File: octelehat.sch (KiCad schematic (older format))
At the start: 32 parts, among them J1 GROVE-CONNECTOR-DIP-90D_4P-2.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, J2 GROVE-CONNECTOR-DIP-90D_4P-2.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, J3 GROVE-CONNECTOR-DIP-90D_4P-2.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, P1 CONN_02X20, P2 CONN_01X02, P3 CONN_01X02, U1 MAX31855KASA, U2 ADS1015, U3 MAX31855KASA

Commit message: work in progress
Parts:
- P1: MFPN F185-1220A0BSYA1 -> (none); MPN (none) -> F185-1220A0BSYA1
- U2: MPN (none) -> ADS1015IDGSR; Manufacturer (none) -> Texas Instruments
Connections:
- net +3V3: now also J1.3, J2.3
- net GND: now also J1.4, J2.4
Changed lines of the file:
@@
 F 3 "https://statics3.seeedstudio.com/images/opl/datasheet/320030087.pdf" H 2400 1400 50  0001 C CNN
 F 4 "YXCON" H 2400 2350 60  0001 C CNN "Manufacturer"
-F 5 "F185-1220A0BSYA1" H 2400 1300 50  0000 C CNN "MFPN"
+F 5 "F185-1220A0BSYA1" H 2400 1300 50  0000 C CNN "MPN"
 	1    2400 2350
 	1    0    0    -1
@@
 F 2 "Housings_SSOP:TSSOP-10_3x3mm_Pitch0.5mm" H 7550 4100 60  0001 C CNN
 F 3 "http://www.ti.com/lit/ds/symlink/ads1015.pdf" H 7550 4100 60  0001 C CNN
+F 4 "ADS1015IDGSR" H 7550 4100 60  0001 C CNN "MPN"
+F 5 "Texas Instruments" H 7550 4100 60  0001 C CNN "Manufacturer"
 	1    7550 4100
 	1    0    0    -1
@@
 	3850 7400 3850 6750
 Wire Wire Line
-	3850 6750 4000 6750
-Wire Wire Line
-	4000 6650 3800 6650
+	3400 6750 4000 6750
+Wire Wire Line
+	3400 6650 4000 6650
 Wire Wire Line
 	3800 6650 3800 7300
@@
 Wire Wire Line
 	8100 5900 10450 5900
+Connection ~ 3800 6650
+Connection ~ 3850 6750
+Text Label 3400 6650 2    60   ~ 0
++3V3
+Text Label 3400 6750 2    60   ~ 0
+GND
 $EndSCHEMATC

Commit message: rev1 routing
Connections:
- net at C8.2, C9.1, R7.1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: now also R8.1; no longer J3.2
- net at C7.2, C8.1, R7.2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: now also J3.2; no longer R8.1
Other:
- moved on the sheet: R8
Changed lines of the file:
@@
 	8550 4200 8550 4850
 Wire Wire Line
-	8550 4850 9500 4850
+	8550 4850 10250 4850
 Wire Wire Line
 	8800 4800 8800 4900
@@
 	9300 5250 9300 5200
 Connection ~ 9300 5250
-Wire Wire Line
-	9800 4850 10350 4850
 $Comp
 L GND #PWR018
@@
 Text Label 2650 1400 0    60   ~ 0
 5V
-Wire Wire Line
-	8450 5250 10250 5250
 Wire Notes Line
 	3800 700  950  700
@@
 $EndComp
 Wire Wire Line
-	10250 5250 10250 5700
-Wire Wire Line
 	10250 5700 10450 5700
-Wire Wire Line
-	10350 4850 10350 5600
 Wire Wire Line
 	10350 5600 10450 5600
@@
 L SMD-RES-30K-1%-1_10W_0603_ R8
 U 1 1 58E635B8
-P 9650 4850
-F 0 "R8" H 9500 4900 45  0000 L BNN
-F 1 "SMD-RES-30K-1%-1_10W_0603_" H 9650 4900 45  0000 L BNN
-F 2 "SeeedOPL-Resistor-2016:R0603" H 9650 4850 40  0001 C CNN
-F 3 "" H 9650 4850 40  0001 C CNN
-F 4 "RC0603FR-0730KL" H 9680 5000 20  0001 C CNN "MPN"
-F 5 "301010202" H 9680 5000 20  0001 C CNN "SKU"
-	1    9650 4850
+P 9650 5250
+F 0 "R8" H 9500 5300 45  0000 L BNN
+F 1 "SMD-RES-30K-1%-1_10W_0603_" H 9650 5300 45  0000 L BNN
+F 2 "SeeedOPL-Resistor-2016:R0603" H 9650 5250 40  0001 C CNN
+F 3 "" H 9650 5250 40  0001 C CNN
+F 4 "RC0603FR-0730KL" H 9680 5400 20  0001 C CNN "MPN"
+F 5 "301010202" H 9680 5400 20  0001 C CNN "SKU"
+	1    9650 5250
 	1    0    0    -1
 $EndComp
@@
 Text Label 3400 6750 2    60   ~ 0
 GND
+Wire Wire Line
+	8450 5250 9500 5250
+Wire Wire Line
+	9800 5250 10350 5250
+Wire Wire Line
+	10350 5250 10350 5600
+Wire Wire Line
+	10250 4850 10250 5700
 $EndSCHEMATC

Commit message: revised
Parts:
- C1, C10, C2, C3, C4, C6, C7, C8, C9: OPL 302010024 -> (none); SKU (none) -> 302010024
- C11, C5: OPL 302010006 -> (none); SKU (none) -> 302010006
- FB1, FB2, FB3, FB4: OPL 303030001 -> (none); SKU (none) -> 303030001
- J1, J2, J3: OPL 320110034 -> (none); SKU (none) -> 320110034
- P1: SKU (none) -> 320030015
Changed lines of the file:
@@
 Sheet 1 1
 Title "Overclocking Telemetry HAT for Raspberry Pi 3"
-Date "2017-04-05"
-Rev "v1"
+Date "2017-04-07"
+Rev "1"
 Comp "moonpunch.org"
 Comment1 "CERN OHL 1.2"
@@
 F 4 "YXCON" H 2400 2350 60  0001 C CNN "Manufacturer"
 F 5 "F185-1220A0BSYA1" H 2400 1300 50  0000 C CNN "MPN"
+F 6 "320030015" H 2400 2350 60  0001 C CNN "SKU"
 	1    2400 2350
 	1    0    0    -1
@@
 F 4 "Yageo" H 6550 2000 60  0001 C CNN "Manufacturer"
 F 5 "CC0402KRX7R9BB103" H 6550 2000 60  0001 C CNN "MPN"
-F 6 "302010006" H 6550 2000 60  0001 C CNN "OPL"
+F 6 "302010006" H 6550 2000 60  0001 C CNN "SKU"
 	1    6550 2000
 	-1   0    0    -1
@@
 F 4 "Yageo" H 6100 1400 60  0001 C CNN "Manufacturer"
 F 5 "CC0402KRX7R8BB104" H 6100 1400 60  0001 C CNN "MPN"
-F 6 "302010024" H 6100 1400 60  0001 C CNN "OPL"
+F 6 "302010024" H 6100 1400 60  0001 C CNN "SKU"
 	1    6100 1400
 	0    -1   -1   0
@@
 F 4 "Murata" H 6900 1800 60  0001 C CNN "Manufacturer"
 F 5 "BLM18AG121SN1D" H 6750 1550 50  0000 C CNN "MPN"
-F 6 "303030001" H 6900 1800 60  0001 C CNN "OPL"
+F 6 "303030001" H 6900 1800 60  0001 C CNN "SKU"
 F 7 "Taiyo Yuden" H 6900 1800 60  0001 C CNN "Manufacturer2"
 F 8 "BK1608HW121-T" H 6800 1550 40  0001 C CNN "MPN2"
@@
 F 4 "Murata" H 6900 2200 60  0001 C CNN "Manufacturer"
 F 5 "BLM18AG121SN1D" H 6900 2200 60  0001 C CNN "MPN"
-F 6 "303030001" H 6900 2200 60  0001 C CNN "OPL"
+F 6 "303030001" H 6900 2200 60  0001 C CNN "SKU"
 F 7 "Taiyo Yuden" H 6900 2200 60  0001 C CNN "Manufacturer2"
 F 8 "BK1608HW121-T" H 6800 1950 40  0001 C CNN "MPN2"
@@
 F 4 "Murata" H 10250 1800 60  0001 C CNN "Manufacturer"
 F 5 "BLM18AG121SN1D" H 10050 1550 50  0000 C CNN "MPN"
-F 6 "303030001" H 10250 1800 60  0001 C CNN "OPL"
+F 6 "303030001" H 10250 1800 60  0001 C CNN "SKU"
 F 7 "Taiyo Yuden" H 10250 1800 60  0001 C CNN "Manufacturer2"
 F 8 "BK1608HW121-T" H 10150 1550 40  0001 C CNN "MPN2"
@@
 F 4 "Murata" H 10250 2200 60  0001 C CNN "Manufacturer"
 F 5 "BLM18AG121SN1D" H 10250 2200 60  0001 C CNN "MPN"
-F 6 "303030001" H 10250 2200 60  0001 C CNN "OPL"
+F 6 "303030001" H 10250 2200 60  0001 C CNN "SKU"
 F 7 "Taiyo Yuden" H 10250 2200 60  0001 C CNN "Manufacturer2"
 F 8 "BK1608HW121-T" H 10150 1950 40  0001 C CNN "MPN2"
@@
 F 4 "Yageo" H 9900 2000 60  0001 C CNN "Manufacturer"
 F 5 "CC0402KRX7R9BB103" H 9900 2000 60  0001 C CNN "MPN"
-F 6 "302010006" H 9900 2000 60  0001 C CNN "OPL"
+F 6 "302010006" H 9900 2000 60  0001 C CNN "SKU"
 	1    9900 2000
 	-1   0    0    -1
@@
 F 4 "Yageo" H 9450 1400 60  0001 C CNN "Manufacturer"
 F 5 "CC0402KRX7R8BB104" H 9450 1400 60  0001 C CNN "MPN"
-F 6 "302010024" H 9450 1400 60  0001 C CNN "OPL"
+F 6 "302010024" H 9450 1400 60  0001 C CNN "SKU"
 	1    9450 1400
 	0    -1   -1   0
@@
 F 4 "Yageo" H 6150 4800 60  0001 C CNN "Manufacturer"
 F 5 "CC0402KRX7R8BB104" H 6150 4800 60  0001 C CNN "MPN"
-F 6 "302010024" H 6150 4800 60  0001 C CNN "OPL"
+F 6 "302010024" H 6150 4800 60  0001 C CNN "SKU"
 	1    6150 4800
 	1    0    0    -1
@@
 F 4 "Yageo" H 8800 4250 60  0001 C CNN "Manufacturer"
 F 5 "CC0402KRX7R8BB104" H 8800 4250 60  0001 C CNN "MPN"
-F 6 "302010024" H 8800 4250 60  0001 C CNN "OPL"
+F 6 "302010024" H 8800 4250 60  0001 C CNN "SKU"
 	1    8800 4250
 	1    0    0    -1
@@
 F 4 "Taifeng" H 10600 5750 60  0001 C CNN "Manufacturer"
 F 5 "1125R-4P" H 10600 5750 60  0001 C CNN "MPN"
-F 6 "320110034" H 10630 5900 20  0001 C CNN "OPL"
+F 6 "320110034" H 10630 5900 20  0001 C CNN "SKU"
 	1    10600 5750
 	1    0    0    -1
@@
 F 4 "Yageo" H 8800 4650 60  0001 C CNN "Manufacturer"
 F 5 "CC0402KRX7R8BB104" H 8800 4650 60  0001 C CNN "MPN"
-F 6 "302010024" H 8800 4650 60  0001 C CNN "OPL"
+F 6 "302010024" H 8800 4650 60  0001 C CNN "SKU"
 	1    8800 4650
 	1    0    0    -1
@@
 F 4 "Yageo" H 8800 5050 60  0001 C CNN "Manufacturer"
 F 5 "CC0402KRX7R8BB104" H 8800 5050 60  0001 C CNN "MPN"
-F 6 "302010024" H 8800 5050 60  0001 C CNN "OPL"
+F 6 "302010024" H 8800 5050 60  0001 C CNN "SKU"
 	1    8800 5050
 	1    0    0    -1
@@
 F 4 "Yageo" H 8800 5450 60  0001 C CNN "Manufacturer"
 F 5 "CC0402KRX7R8BB104" H 8800 5450 60  0001 C CNN "MPN"
-F 6 "302010024" H 8800 5450 60  0001 C CNN "OPL"
+F 6 "302010024" H 8800 5450 60  0001 C CNN "SKU"
 	1    8800 5450
 	1    0    0    -1
@@
 F 4 "Yageo" H 6150 5200 60  0001 C CNN "Manufacturer"
 F 5 "CC0402KRX7R8BB104" H 6150 5200 60  0001 C CNN "MPN"
-F 6 "302010024" H 6150 5200 60  0001 C CNN "OPL"
+F 6 "302010024" H 6150 5200 60  0001 C CNN "SKU"
 	1    6150 5200
 	1    0    0    -1
@@
 F 4 "Yageo" H 6150 5600 60  0001 C CNN "Manufacturer"
 F 5 "CC0402KRX7R8BB104" H 6150 5600 60  0001 C CNN "MPN"
-F 6 "302010024" H 6150 5600 60  0001 C CNN "OPL"
+F 6 "302010024" H 6150 5600 60  0001 C CNN "SKU"
 	1    6150 5600
 	1    0    0    -1
@@
 F 4 "Taifeng" H 4150 6600 60  0001 C CNN "Manufacturer"
 F 5 "1125R-4P" H 4150 6600 60  0001 C CNN "MPN"
-F 6 "320110034" H 4180 6750 20  0001 C CNN "OPL"
+F 6 "320110034" H 4180 6750 20  0001 C CNN "SKU"
 	1    4150 6600
 	1    0    0    -1
@@
 F 4 "Taifeng" H 4150 7250 60  0001 C CNN "Manufacturer"
 F 5 "1125R-4P" H 4150 7250 60  0001 C CNN "MPN"
-F 6 "320110034" H 4180 7400 20  0001 C CNN "OPL"
+F 6 "320110034" H 4180 7400 20  0001 C CNN "SKU"
 	1    4150 7250
 	1    0    0    -1

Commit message: design update
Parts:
- FB1, FB2, FB3, FB4: footprint Resistors_SMD:R_0603_HandSoldering -> SeeedOPL-Inductor-2016:L0603
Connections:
- net at C3.2, C4.1, R3.1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: now also J3.2; no longer J3.4
- net at C7.2, C8.1, R7.2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: now also J3.4; no longer J3.2
- net at J3.1: now also R4.2; no longer R8.2
- net at J3.3: now also R8.2; no longer R4.2

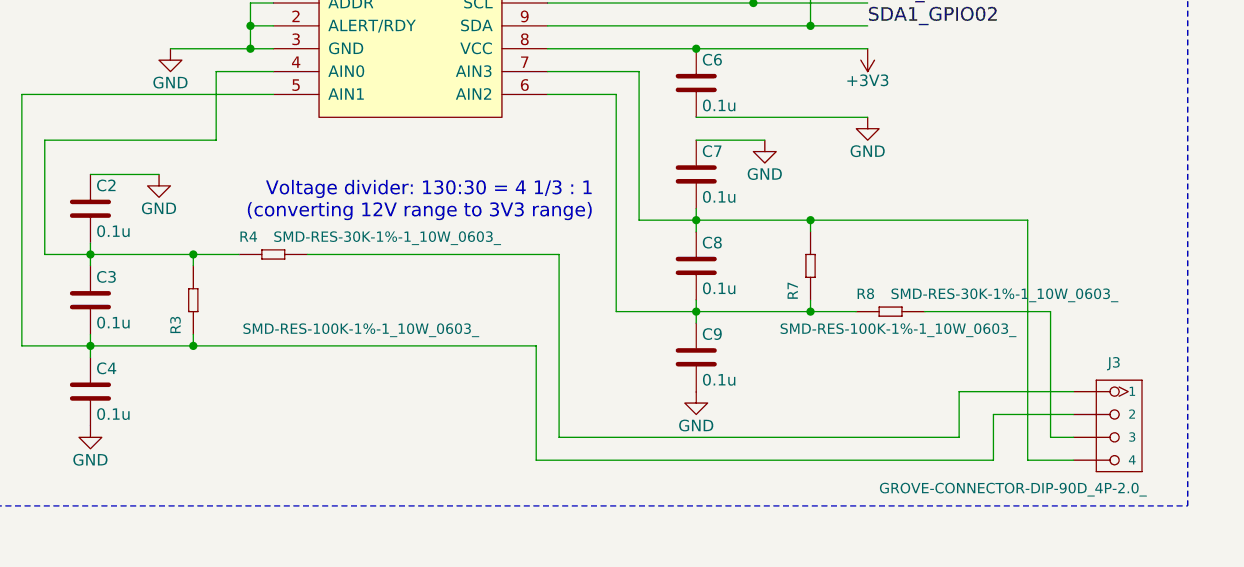
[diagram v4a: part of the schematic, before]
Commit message: update voltage divider part of circuit
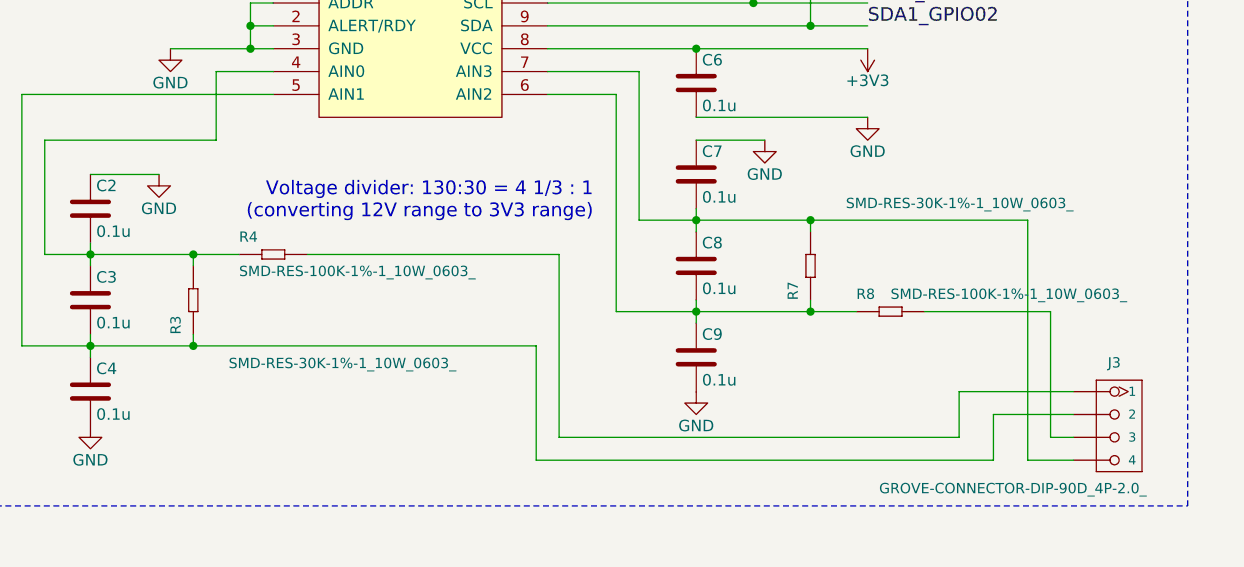
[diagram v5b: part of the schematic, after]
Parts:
- removed R3, R7: SMD-RES-100K-1%-1_10W_0603_, SeeedOPL-Resistor-2016:R0603, symbol SMD-RES-100K-1%-1_10W_0603_
- removed R4, R8: SMD-RES-30K-1%-1_10W_0603_, SeeedOPL-Resistor-2016:R0603, symbol SMD-RES-30K-1%-1_10W_0603_
- added R3, R7: SMD-RES-30K-1%-1_10W_0603_, symbol SMD-RES-30K-1%-1_10W_0603_
- added R4, R8: SMD-RES-100K-1%-1_10W_0603_, symbol SMD-RES-100K-1%-1_10W_0603_
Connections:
- net at C2.2, C3.1, U2.4 (AIN0): now also R3.2, R4.1
- net at C3.2, C4.1, J3.2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: now also R3.1
- net at C8.2, C9.1, U2.6 (AIN2): now also R7.1, R8.1
- net at C7.2, C8.1, J3.4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: now also R7.2
- net at J3.1: now also R4.2
- net at J3.3: now also R8.2
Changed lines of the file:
@@
 Sheet 1 1
 Title "Overclocking Telemetry HAT for Raspberry Pi 3"
-Date "2017-04-10"
-Rev "1"
+Date "2017-05-19"
+Rev "2"
 Comp "moonpunch.org"
 Comment1 "CERN OHL 1.2"
@@
 $EndComp
 $Comp
-L SMD-RES-30K-1%-1_10W_0603_ R4
-U 1 1 58E62ECC
-P 6950 5000
-F 0 "R4" H 6800 5050 45  0000 L BNN
-F 1 "SMD-RES-30K-1%-1_10W_0603_" H 6950 5050 45  0000 L BNN
-F 2 "SeeedOPL-Resistor-2016:R0603" H 6950 5000 40  0001 C CNN
-F 3 "" H 6950 5000 40  0001 C CNN
-F 4 "RC0603FR-0730KL" H 6980 5150 20  0001 C CNN "MPN"
-F 5 "301010202" H 6980 5150 20  0001 C CNN "SKU"
-	1    6950 5000
-	1    0    0    -1
-$EndComp
-$Comp
-L SMD-RES-100K-1%-1_10W_0603_ R3
-U 1 1 58E63018
-P 6600 5200
-F 0 "R3" H 6450 5250 45  0000 L BNN
-F 1 "SMD-RES-100K-1%-1_10W_0603_" V 6500 3950 45  0000 L BNN
-F 2 "SeeedOPL-Resistor-2016:R0603" H 6600 5200 40  0001 C CNN
-F 3 "https://statics3.seeedstudio.com/images/opl/datasheet/301010196.pdf" H 6600 5200 40  0001 C CNN
-F 4 "RC0603FR-07100KL" H 6630 5350 20  0001 C CNN "MPN"
-F 5 "301010196" H 6630 5350 20  0001 C CNN "SKU"
-	1    6600 5200
-	0    -1   -1   0
-$EndComp
-$Comp
-L SMD-RES-100K-1%-1_10W_0603_ R7
-U 1 1 58E634F7
-P 9300 5050
-F 0 "R7" H 9150 5100 45  0000 L BNN
-F 1 "SMD-RES-100K-1%-1_10W_0603_" V 9050 4150 45  0000 L BNN
-F 2 "SeeedOPL-Resistor-2016:R0603" H 9300 5050 40  0001 C CNN
-F 3 "https://statics3.seeedstudio.com/images/opl/datasheet/301010196.pdf" H 9300 5050 40  0001 C CNN
-F 4 "RC0603FR-07100KL" H 9330 5200 20  0001 C CNN "MPN"
-F 5 "301010196" H 9330 5200 20  0001 C CNN "SKU"
-	1    9300 5050
-	0    -1   -1   0
-$EndComp
-$Comp
-L SMD-RES-30K-1%-1_10W_0603_ R8
-U 1 1 58E635B8
-P 9650 5250
-F 0 "R8" H 9500 5300 45  0000 L BNN
-F 1 "SMD-RES-30K-1%-1_10W_0603_" H 9650 5300 45  0000 L BNN
-F 2 "SeeedOPL-Resistor-2016:R0603" H 9650 5250 40  0001 C CNN
-F 3 "" H 9650 5250 40  0001 C CNN
-F 4 "RC0603FR-0730KL" H 9680 5400 20  0001 C CNN "MPN"
-F 5 "301010202" H 9680 5400 20  0001 C CNN "SKU"
-	1    9650 5250
-	1    0    0    -1
-$EndComp
-$Comp
 L SMD-RES-10K-1%-1_10W_0603_ R5
 U 1 1 58E63772
@@
 Wire Wire Line
 	10100 5700 10450 5700
+$Comp
+L SMD-RES-100K-1%-1_10W_0603_ R4
+U 1 1 591F25A1
+P 6950 5000
+F 0 "R4" H 6800 5050 45  0000 L BNN
+F 1 "SMD-RES-100K-1%-1_10W_0603_" H 6800 4900 45  0000 L BNN
+F 2 "" H 6950 5000 40  0001 C CNN
+F 3 "" H 6950 5000 40  0001 C CNN
+F 4 "RC0603FR-07100KL" H 6980 5150 20  0001 C CNN "MPN"
+F 5 "301010196" H 6980 5150 20  0001 C CNN "SKU"
+	1    6950 5000
+	1    0    0    -1
+$EndComp
+$Comp
+L SMD-RES-100K-1%-1_10W_0603_ R8
+U 1 1 591F263A
+P 9650 5250
+F 0 "R8" H 9500 5300 45  0000 L BNN
+F 1 "SMD-RES-100K-1%-1_10W_0603_" H 9650 5300 45  0000 L BNN
+F 2 "" H 9650 5250 40  0001 C CNN
+F 3 "" H 9650 5250 40  0001 C CNN
+F 4 "RC0603FR-07100KL" H 9680 5400 20  0001 C CNN "MPN"
+F 5 "301010196" H 9680 5400 20  0001 C CNN "SKU"
+	1    9650 5250
+	1    0    0    -1
+$EndComp
+$Comp
+L SMD-RES-30K-1%-1_10W_0603_ R3
+U 1 1 591F26AD
+P 6600 5200
+F 0 "R3" H 6450 5250 45  0000 L BNN
+F 1 "SMD-RES-30K-1%-1_10W_0603_" V 6350 4050 45  0000 L BNN
+F 2 "" H 6600 5200 40  0001 C CNN
+F 3 "" H 6600 5200 40  0001 C CNN
+F 4 "RC0603FR-0730KL" H 6630 5350 20  0001 C CNN "MPN"
+F 5 "301010202" H 6630 5350 20  0001 C CNN "SKU"
+	1    6600 5200
+	0    -1   -1   0
+$EndComp
+$Comp
+L SMD-RES-30K-1%-1_10W_0603_ R7
+U 1 1 591F2730
+P 9300 5050
+F 0 "R7" H 9150 5100 45  0000 L BNN
+F 1 "SMD-RES-30K-1%-1_10W_0603_" V 9600 3900 45  0000 L BNN
+F 2 "" H 9300 5050 40  0001 C CNN
+F 3 "" H 9300 5050 40  0001 C CNN
+F 4 "RC0603FR-0730KL" H 9330 5200 20  0001 C CNN "MPN"
+F 5 "301010202" H 9330 5200 20  0001 C CNN "SKU"
+	1    9300 5050
+	0    -1   -1   0
+$EndComp
 $EndSCHEMATC

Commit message: updated rev2
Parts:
- P1: MPN F185-1220A0BSYA1 -> REF-182684-02; Manufacturer YXCON -> Toby Electronics; SKU 320030015 -> (none)
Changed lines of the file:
@@
 F 1 "CONN_02X20" V 2400 2350 50  0000 C CNN
 F 2 "Socket_Strips:Socket_Strip_Straight_2x20_Pitch2.54mm" H 2400 1300 50  0001 C CNN
-F 3 "https://statics3.seeedstudio.com/images/opl/datasheet/320030087.pdf" H 2400 1400 50  0001 C CNN
-F 4 "YXCON" H 2400 2350 60  0001 C CNN "Manufacturer"
-F 5 "F185-1220A0BSYA1" H 2400 1300 50  0000 C CNN "MPN"
-F 6 "320030015" H 2400 2350 60  0001 C CNN "SKU"
+F 3 "https://www.toby.co.uk/datasheets/section4/REF-18xxxx-0x.pdf?revDate=17112016113546" H 2400 1400 50  0001 C CNN
+F 4 "Toby Electronics" H 2400 2350 60  0001 C CNN "Manufacturer"
+F 5 "REF-182684-02" H 2400 1300 50  0000 C CNN "MPN"
 	1    2400 2350
 	1    0    0    -1
